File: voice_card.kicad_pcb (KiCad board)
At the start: 2 copper layers, 79.2 x 7.9 mm, 209 parts, among them J1 PCI_11_49, Q1 MMBF4391LT1G, Q10 DMMT3906, Q11 BC857BS, Q2 2N3904, Q3 BCM847, Q4 DMMT3904, Q5 DMMT3906, Q6 MMBF4391LT1G, Q7 BCM847, Q8 2N3904, Q9 DMMT3904, U1 TL074-, U10 TL072-, U11 TL074-, U12 NE555, U13 LM311M, U14 CD4052, U15 TL072-, U16 TL072-, U17 LM13700, U18 LM13700, U19 LM13700, U2 TL074-, U20 TL072-, U3 NE555, U4 LF351, U5 TL072-, U6 LM311M, U7 CD4052, U8 TL074-, U9 LF351

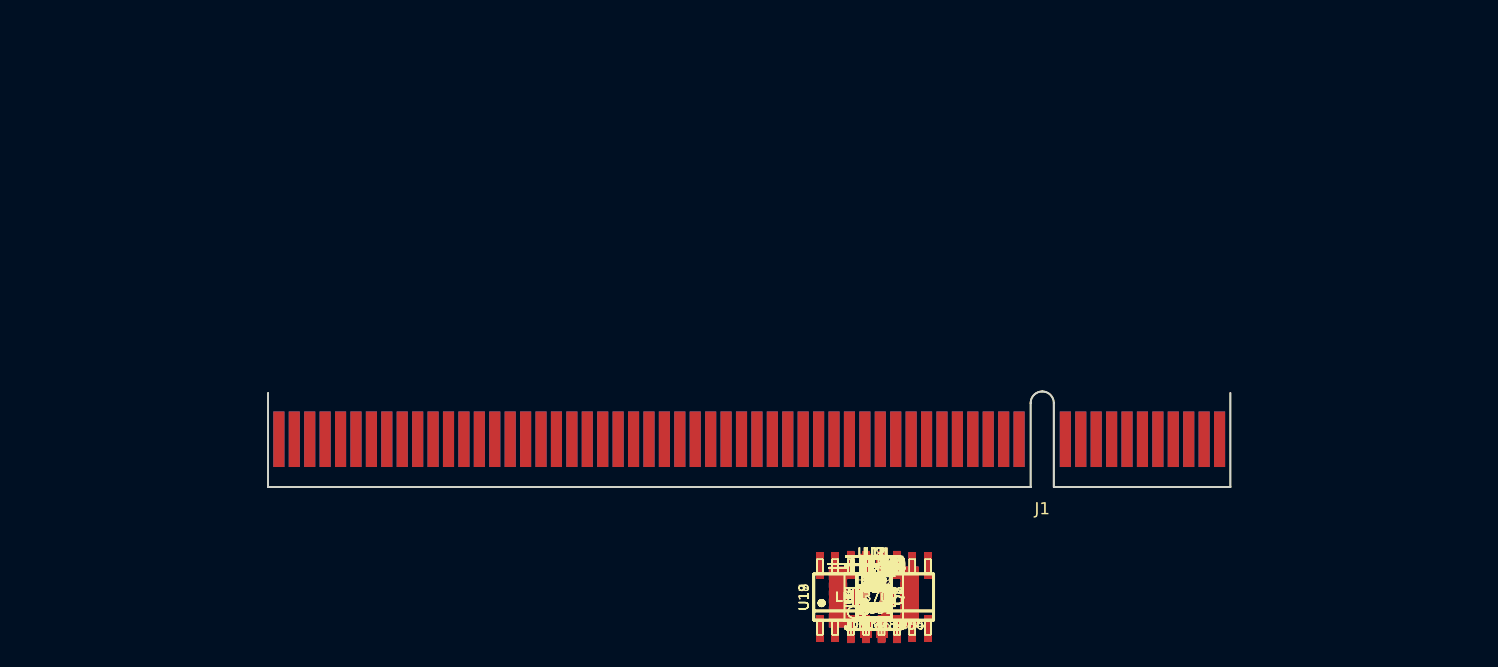
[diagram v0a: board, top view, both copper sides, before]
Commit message: laying out and routing VCO1 core
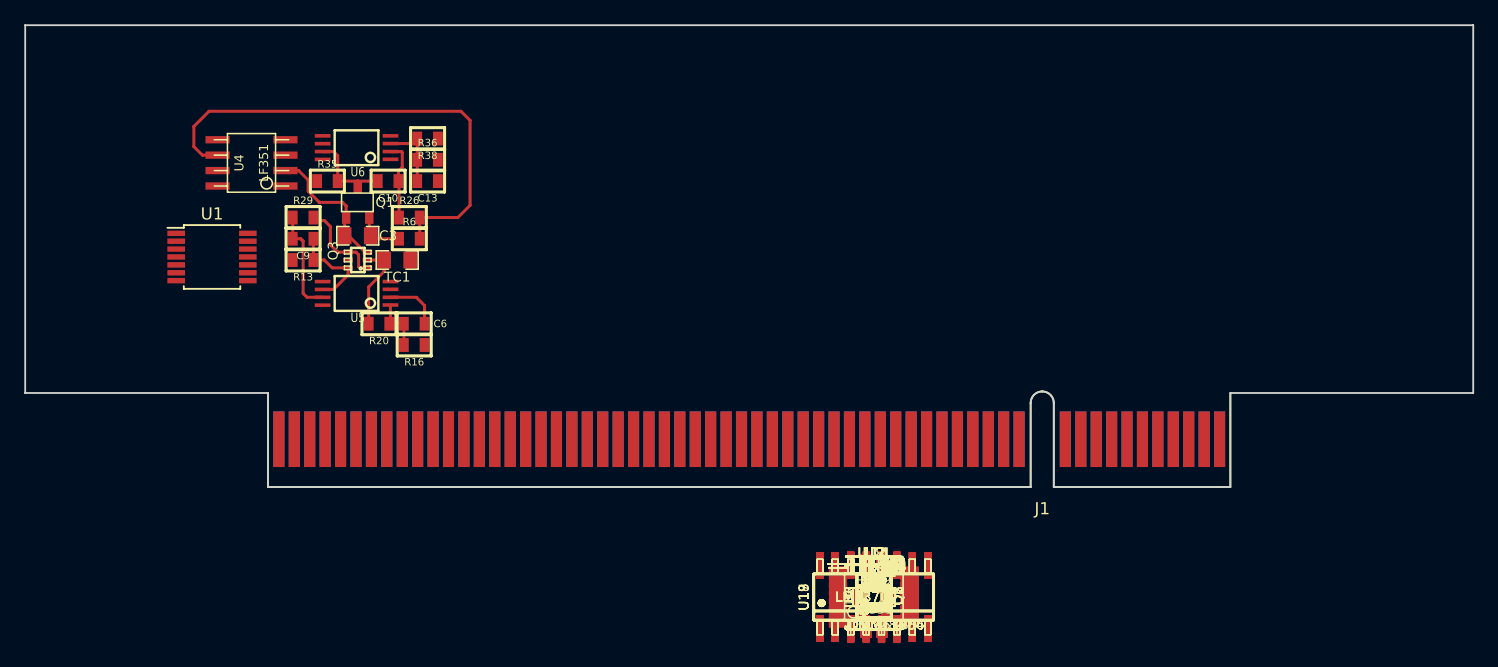
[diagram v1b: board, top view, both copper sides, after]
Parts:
- moved U4 62.5 mm to (97.2, 69.2), turned to 90 degrees
- moved U1 61.3 mm to (94.0, 77.0)
- moved R35 56.6 mm to (103.5, 70.8)
- moved R29 56.4 mm to (101.5, 73.8)
- moved U6 56.4 mm to (106.0, 68.0), turned to 90 degrees
- moved C9 55.5 mm to (101.5, 75.5), turned to 180 degrees
- moved R13 54.6 mm to (101.5, 77.2), turned to 180 degrees
- moved Q1 53.5 mm to (106.0, 72.5)
- moved R38 52.7 mm to (111.8, 67.2), turned to 180 degrees
- moved C10 52.7 mm to (108.5, 70.8), turned to 180 degrees
- moved C3 51.9 mm to (106.0, 75.2)
- moved R36 51.4 mm to (111.8, 69.0)
- moved Q3 50.8 mm to (106.0, 77.2), turned to 90 degrees
- moved C13 50.2 mm to (111.8, 70.8), turned to 180 degrees
- moved R26 49.4 mm to (110.2, 73.8)
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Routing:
- net Net-(R18-Pad1): track 0.00 -> 40.8 mm
- net Net-(C3-Pad1): track 0.00 -> 11.7 mm
- net Net-(C9-Pad2): track 0.00 -> 8.73 mm
- net Net-(C9-Pad1): track 0.00 -> 8.04 mm
- net Net-(Q3-Pad1): track 0.00 -> 7.56 mm
- net Net-(C10-Pad2): track 0.00 -> 7.25 mm
- net Net-(Q3-Pad2): track 0.00 -> 7.15 mm
- net Net-(C10-Pad1): track 0.00 -> 6.51 mm
- net Net-(C13-Pad2): track 0.00 -> 5.87 mm
- net VCO1_PITCH_CV: track 0.00 -> 4.59 mm
- net Net-(C6-Pad1): track 0.00 -> 4.53 mm
- net Net-(C3-Pad2): track 0.00 -> 3.96 mm
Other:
- board size 79.2 x 7.9 mm -> 119.3 x 38 mm

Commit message: starting to layout waveshapers for VCO1
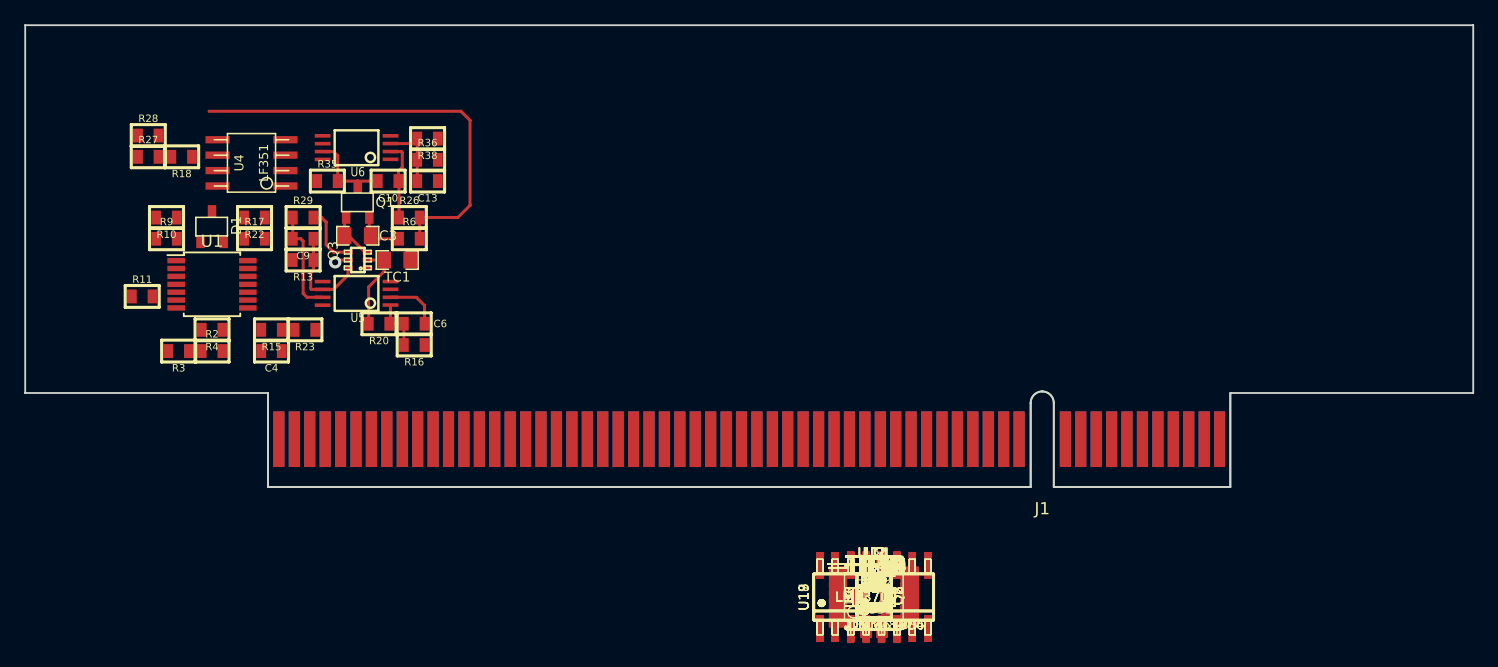
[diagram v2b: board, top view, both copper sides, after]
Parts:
- moved R28 70.8 mm to (88.8, 67.0)
- moved R27 69.9 mm to (88.8, 68.8)
- moved R18 67.6 mm to (91.5, 68.8), turned to 180 degrees
- moved R10 66.1 mm to (90.2, 73.8), turned to 180 degrees
- moved R9 65.3 mm to (90.2, 75.5)
- moved R11 65.1 mm to (88.2, 80.2)
- moved D1 62.5 mm to (94.0, 74.5)
- moved R3 60.7 mm to (91.2, 84.8), turned to 180 degrees
- moved R22 59.8 mm to (97.5, 73.8), turned to 180 degrees
- moved R17 58.9 mm to (97.5, 75.5)
- moved R4 58.8 mm to (94.0, 83.0), turned to 180 degrees
- moved R2 58.1 mm to (94.0, 84.8)
- moved R15 54.3 mm to (98.9, 83.0), turned to 180 degrees
- moved C4 53.6 mm to (98.9, 84.8), turned to 180 degrees
- moved R23 51.8 mm to (101.6, 83.0), turned to 180 degrees
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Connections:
- U1 pad 10: GND -> Net-(R2-Pad1)
- U1 pad 12: Net-(R2-Pad1) -> GND
- U1 pad 13: VCO1_SAW -> Net-(C4-Pad1)
- U1 pad 14: VCO1_PULSE -> VCO1_TRI
- U1 pad 8: VCO1_TRI -> VCO1_PULSE
- U1 pad 9: Net-(C4-Pad1) -> VCO1_SAW
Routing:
- net Net-(C3-Pad1): track 11.7 -> 3.97 mm
- net Net-(R18-Pad1): track 40.8 -> 35.1 mm
- net Net-(Q3-Pad1): track 7.56 -> 5.12 mm
- net GND: track 0.00 -> 1.14 mm, vias 0 -> 1
- net Net-(C9-Pad1): track 8.04 -> 8.57 mm
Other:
- net class Default: clearance 0.2 -> 0.2032; trace_width 0.25 -> 0.254; via_dia 0.6 -> 1.016; via_drill 0.4 -> 0.508
- net class POWER added: clearance 0.2032, trace_width 0.3048, via_dia 1.016, via_drill 0.508
- rule trace_clearance: 0.2 -> 0.2032

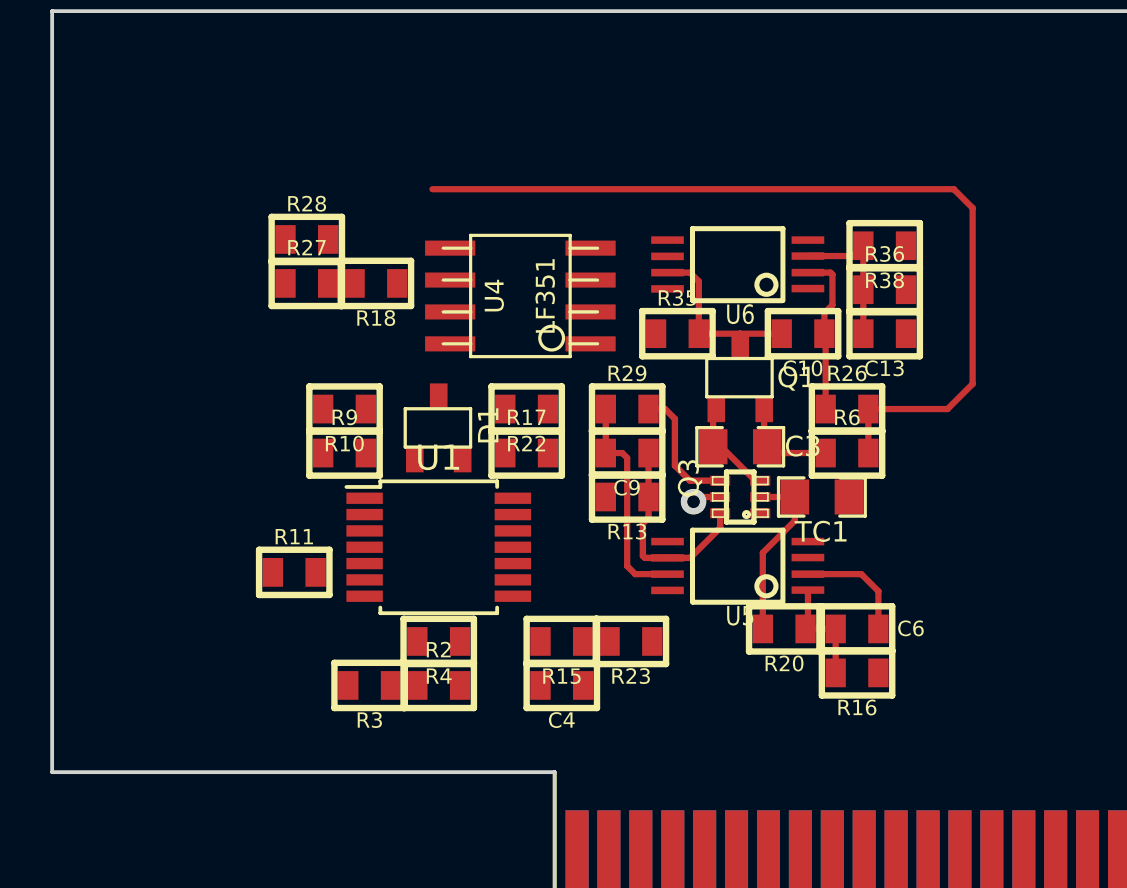
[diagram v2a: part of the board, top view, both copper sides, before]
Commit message: VCO1 more or less routed
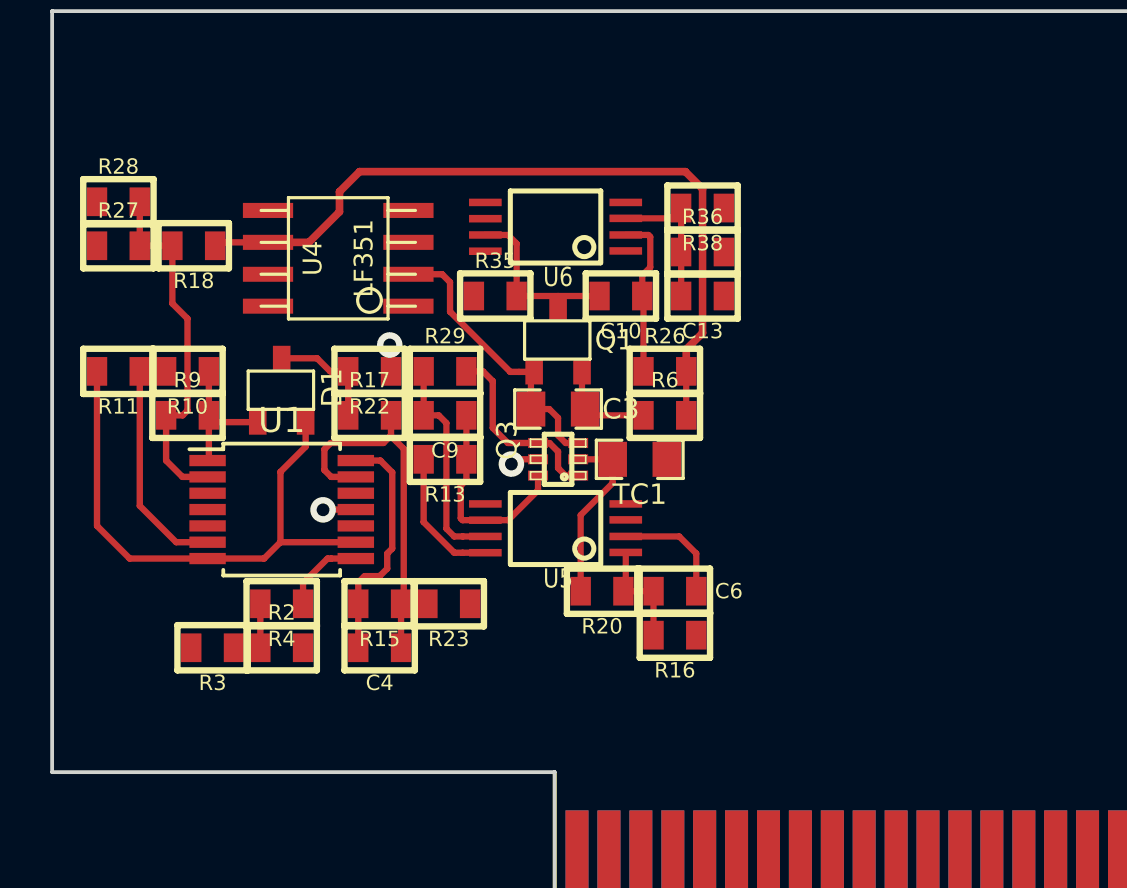
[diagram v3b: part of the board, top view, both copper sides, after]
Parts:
- moved R11 10.6 mm to (81.2, 72.2), turned to 180 degrees
- moved R27 7.65 mm to (81.2, 67.2)
- moved R28 7.65 mm to (81.2, 65.5)
- moved C10 7.40 mm to (101.2, 69.2)
- moved C13 7.40 mm to (104.5, 69.2)
- moved C3 7.40 mm to (98.8, 73.8)
- moved C4 7.40 mm to (91.6, 83.2)
- moved C6 7.40 mm to (103.4, 81.0)
- moved C9 7.40 mm to (94.2, 74.0)
- moved Q1 7.40 mm to (98.8, 71.0)
- moved Q3 7.40 mm to (98.8, 75.8)
- moved R13 7.40 mm to (94.2, 75.8)
- moved R15 7.40 mm to (91.6, 81.5)
- moved R16 7.40 mm to (103.4, 82.8)
- moved R18 7.40 mm to (84.2, 67.2)
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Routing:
- net VCO1_SAW: track 0.00 -> 22.5 mm
- net Net-(C4-Pad1): track 0.00 -> 15.6 mm
- net Net-(R18-Pad2): track 0.00 -> 14.3 mm
- net Net-(R10-Pad2): track 0.00 -> 9.86 mm
- net VCO1_TRI: track 0.00 -> 9.54 mm
- net Net-(C3-Pad1): track 3.97 -> 11.7 mm
- net Net-(D1-Pad2): track 0.00 -> 5.63 mm
- net +12V: track 0.00 -> 5.46 mm
- net Net-(D1-Pad3): track 0.00 -> 4.61 mm
- net Net-(R18-Pad1): track 35.1 -> 30.8 mm
- net VCO1_PULSE: track 0.00 -> 3.33 mm
- net Net-(R2-Pad1): track 0.00 -> 2.80 mm
- net Net-(Q3-Pad1): track 5.12 -> 7.64 mm
- net -12V: track 0.00 -> 2.38 mm, vias 0 -> 2

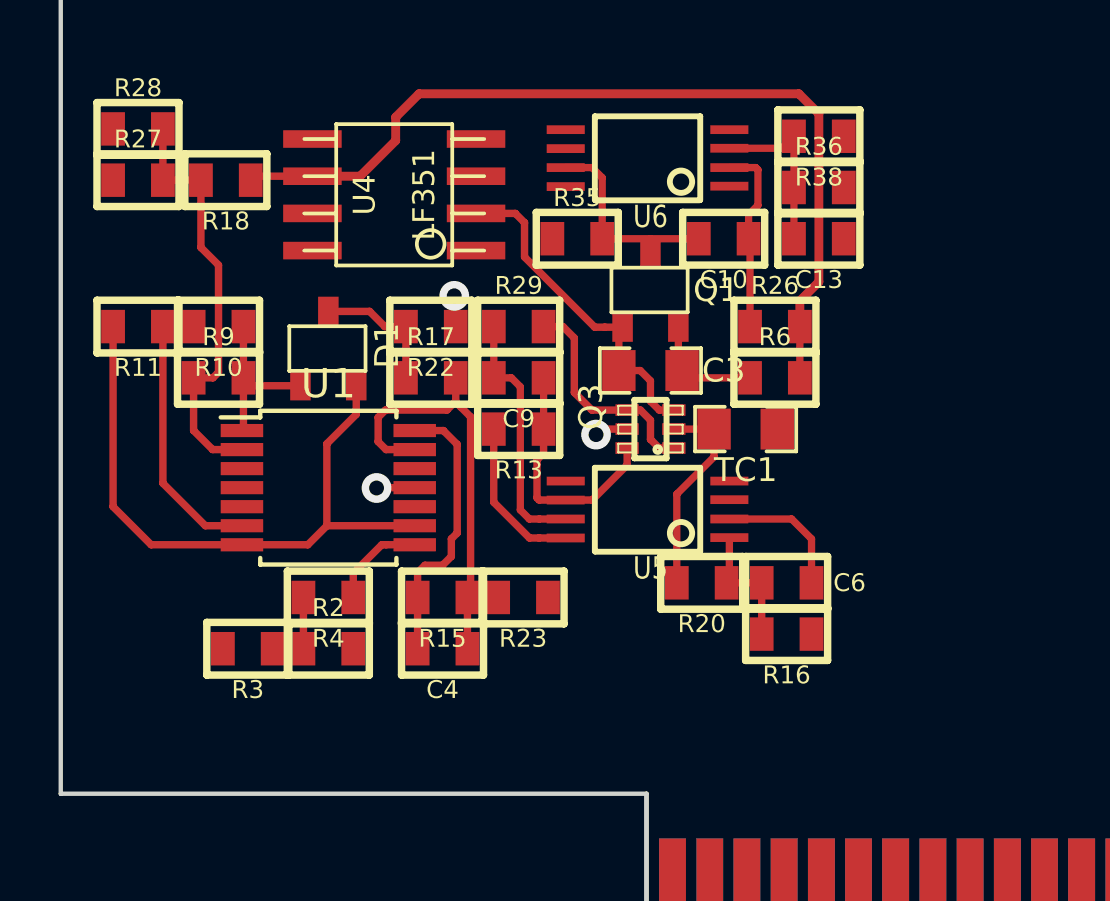
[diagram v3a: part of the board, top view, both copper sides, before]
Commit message: VCO1 basically routed. bringing in and output pins to PCI connector. Need to swap pins to get pinout order correct
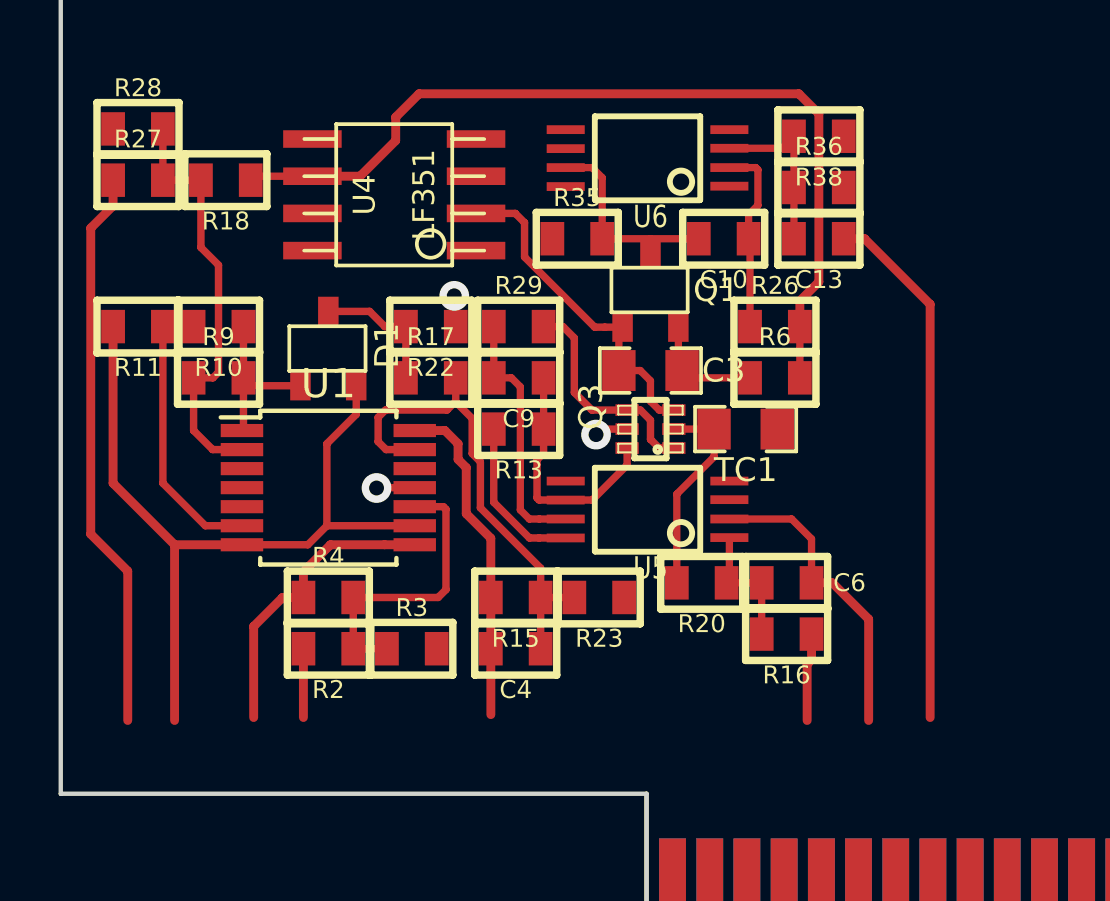
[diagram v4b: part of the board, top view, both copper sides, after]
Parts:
- moved R3 5.60 mm to (90.6, 83.2), turned to 0 degrees
- moved R23 2.60 mm to (97.0, 81.5)
- moved C4 2.50 mm to (94.1, 83.2)
- moved R15 2.50 mm to (94.1, 81.5)
- turned R2 to 180 degrees
- turned R4 to 0 degrees
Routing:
- net VCO1_TRI_SHAPE: track 0.00 -> 19.3 mm
- net VCO1_SYNC_IN: track 0.00 -> 18.0 mm
- net Net-(R2-Pad1): track 2.80 -> 10.0 mm
- net VCO1_PULSE: track 3.33 -> 10.3 mm
- net VCO1_PITCH_CV: track 4.59 -> 10.5 mm
- net VCO1_SAW: track 22.5 -> 28.0 mm
- net VCO1_SCALE: track 0.00 -> 3.01 mm
- net VCO1_PWM_CV: track 0.00 -> 2.35 mm
- net VCO1_TRI: track 9.54 -> 11.4 mm
- net Net-(C4-Pad1): track 15.6 -> 16.7 mm
